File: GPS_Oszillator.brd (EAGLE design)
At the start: 100 x 80 mm, 34 parts, among them IC1 74ACT04D, IC2 7805TV, X1 ST-SMB-V, X2 ST-SMB-V

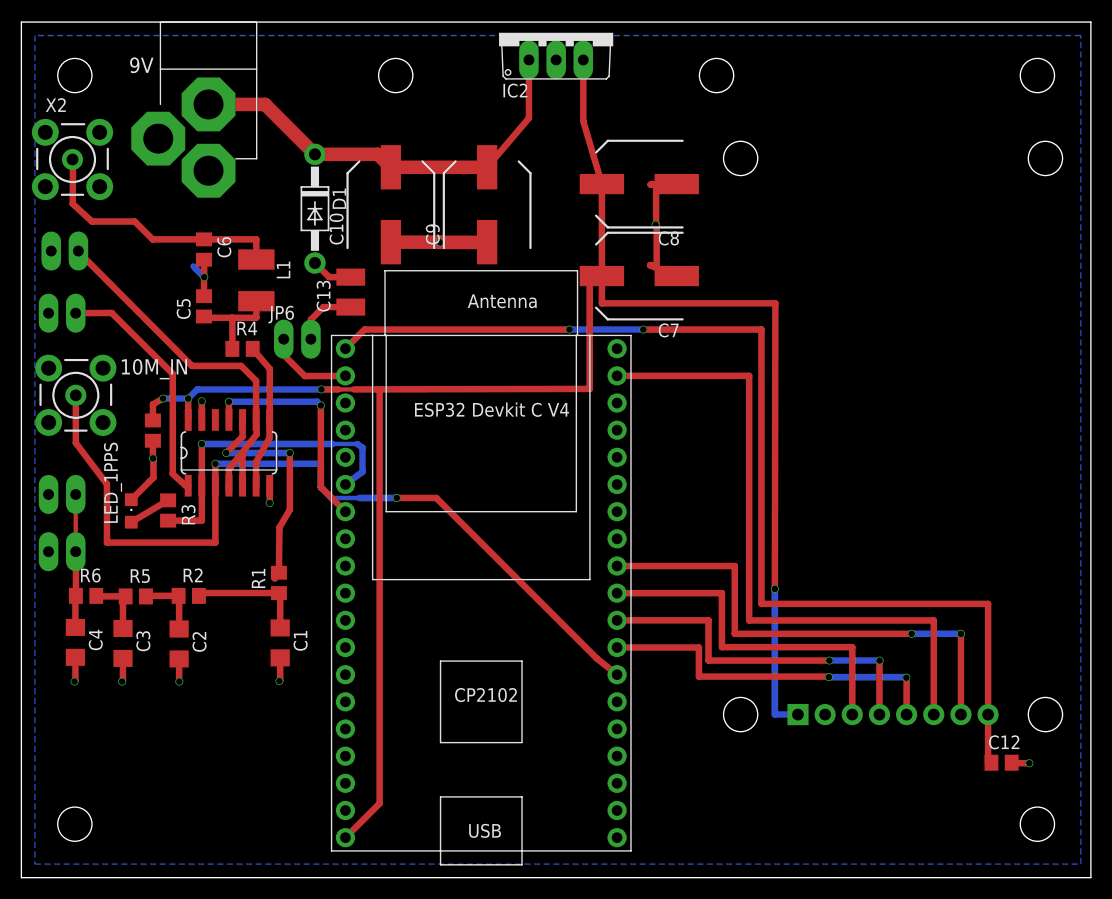
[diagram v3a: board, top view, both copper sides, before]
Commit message: add second power connector and sort out drc errors
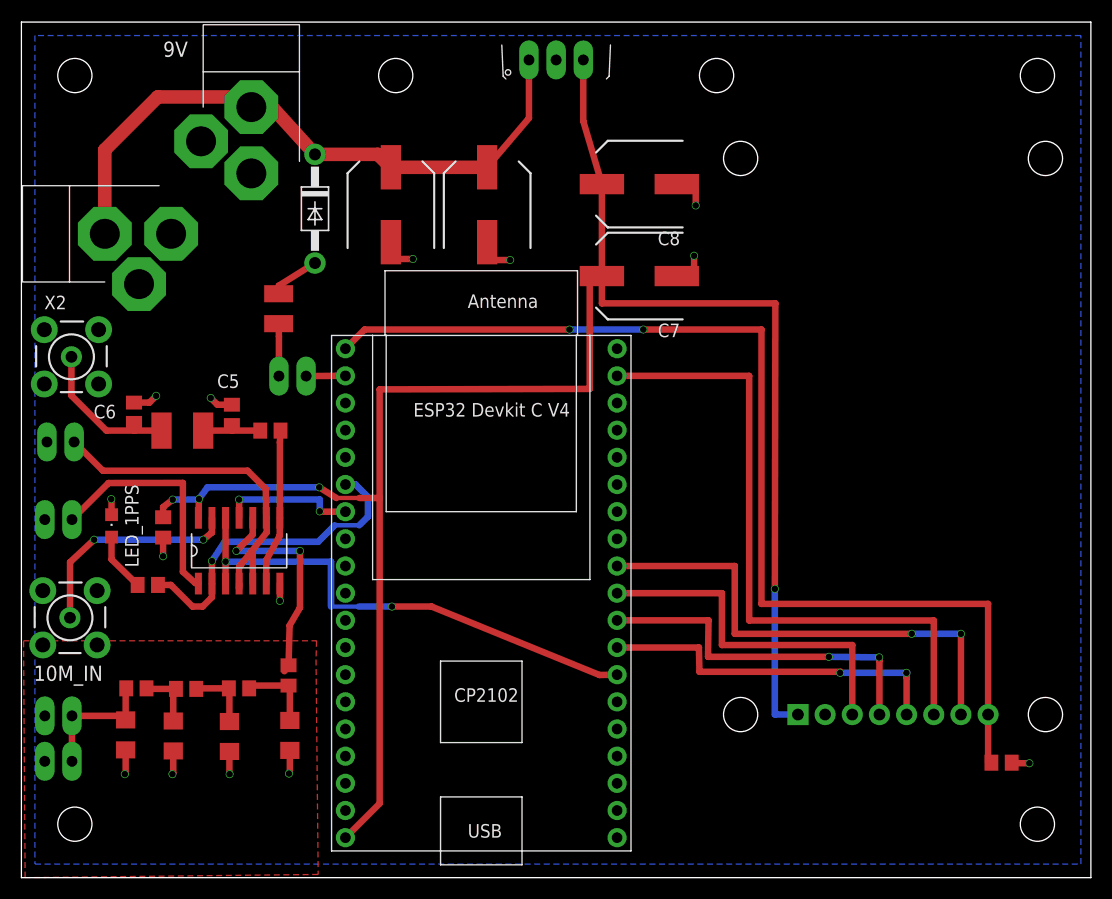
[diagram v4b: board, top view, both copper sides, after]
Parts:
- added U$1: POWERBUCHSE, _Winni:POWERBUCHSE
- moved X1 20.8 mm to (4.54, 24.3)
- moved JP3 20.7 mm to (3.46, 15.1)
- moved JP4 19.6 mm to (3.46, 10.9)
- moved JP5 19.3 mm to (3.46, 33.5)
- moved X2 18.5 mm to (4.68, 48.7)
- moved JP2 17.9 mm to (3.66, 40.7)
- moved C6 16.6 mm to (10.5, 43.5), turned to 90 degrees
- moved L1 15.7 mm to (15.1, 41.8), turned to 0 degrees
- moved C5 10.5 mm to (19.7, 43.3)
- moved C2 9.84 mm to (19.4, 13.2)
- moved R2 9.84 mm to (20.4, 17.7)
- moved R5 9.84 mm to (15.4, 17.6)
- moved R6 9.84 mm to (10.8, 17.7)
- moved C4 9.84 mm to (9.75, 13.3)
- moved C3 9.84 mm to (14.2, 13.2)
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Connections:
- new net N$13: IC1.13, X1.1
- net 10MHZ_IN: now also IC1.12; no longer X1.1
- net GND: now also U$1.2; no longer IC1.13
- net N$12: now also U$1.1
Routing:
- net 10MHZ_IN: track 79.2 -> 48.2 mm
- net N$13: track 0.00 -> 20.9 mm, vias 0 -> 2
- net N$12: track 40.0 -> 60.0 mm
- net GND: track 52.5 -> 40.2 mm, vias 11 -> 14
- net N$9: track 24.5 -> 14.1 mm
- net PWM_OUT: track 21.3 -> 12.8 mm
- net ESP32_EN: track 8.07 -> 3.68 mm
- net N$5: track 10.9 -> 7.10 mm
- net N$10: track 9.40 -> 5.86 mm
- net N$6: track 12.5 -> 15.6 mm
- net N$2: track 36.5 -> 33.5 mm
- net N$8: track 4.00 -> 5.50 mm
- net 5V0: track 179.6 -> 178.5 mm
- net N$4: track 6.04 -> 4.90 mm
- net N$11: track 13.7 -> 14.6 mm
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- added copper zone on layer 1, net GND
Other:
- board text removed: "CMOS"

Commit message: Fix reversed DC Jacks
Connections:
- net GND: now also U$1.1, U$3.1; no longer U$1.2, U$3.2
- net N$12: now also U$1.2, U$3.2; no longer U$1.1, U$3.1
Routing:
- net N$12: track 60.0 -> 44.6 mm
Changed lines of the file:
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@@
 <via x="94.25" y="10.7" extent="1-16" drill="0.6" shape="octagon"/>
 <wire x1="2.48" y1="9.49" x2="2.19" y2="10.88" width="0.6096" layer="1"/>
-<contactref element="U$3" pad="2"/>
+<contactref element="U$3" pad="1"/>
 <contactref element="D1" pad="A"/>
 <contactref element="C13" pad="2"/>
@@
 <wire x1="9.67" y1="9.68" x2="9.75" y2="9.76" width="0.6096" layer="1"/>
 <wire x1="9.75" y1="9.76" x2="9.75" y2="11.95" width="0.6096" layer="1"/>
-<contactref element="U$1" pad="2"/>
+<contactref element="U$1" pad="1"/>
 <via x="8.4" y="35.4" extent="1-16" drill="0.6" shape="octagon"/>
 <wire x1="8.43" y1="33.94" x2="8.43" y2="35.37" width="0.6096" layer="1"/>
@@
 <wire x1="47.46" y1="71.02" x2="47.46" y2="76.46" width="0.6096" layer="1"/>
 <wire x1="34.55" y1="66.42" x2="43.55" y2="66.42" width="1.27" layer="1"/>
-<contactref element="U$3" pad="1"/>
+<contactref element="U$3" pad="2"/>
 <contactref element="D1" pad="C"/>
-<wire x1="21.5" y1="72.05" x2="23.48" y2="72" width="1.27" layer="1"/>
-<wire x1="23.48" y1="72" x2="27.45" y2="67.63" width="1.27" layer="1"/>
+<wire x1="21.5" y1="65.85" x2="23.28" y2="67.63" width="1.27" layer="1"/>
+<wire x1="23.28" y1="67.63" x2="27.45" y2="67.63" width="1.27" layer="1"/>
 <wire x1="27.45" y1="67.63" x2="33.34" y2="67.63" width="1.27" layer="1"/>
 <wire x1="33.34" y1="67.63" x2="34.55" y2="66.42" width="1.27" layer="1"/>
-<contactref element="U$1" pad="1"/>
-<wire x1="7.8" y1="60.2" x2="7.8" y2="68.05" width="1.27" layer="1"/>
-<wire x1="7.8" y1="68.05" x2="12.75" y2="73" width="1.27" layer="1"/>
-<wire x1="12.75" y1="73" x2="20.55" y2="73" width="1.27" layer="1"/>
-<wire x1="20.55" y1="73" x2="21.5" y2="72.05" width="1.27" layer="1"/>
+<contactref element="U$1" pad="2"/>
+<wire x1="14" y1="60.2" x2="15.85" y2="60.2" width="1.27" layer="1"/>
+<wire x1="15.85" y1="60.2" x2="21.5" y2="65.85" width="1.27" layer="1"/>
 </signal>
 <signal name="3V3">
